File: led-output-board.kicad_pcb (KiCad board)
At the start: 2 copper layers, 29 parts, among them J1 DBT50G-9.5-2P, J10 DB301V-3.5-3P-GN, J2 Conn_02x08_Odd_Even, J3 DB301V-3.5-3P-GN, J4 DB301V-3.5-3P-GN, J5 DB301V-3.5-3P-GN, J6 DB301V-3.5-3P-GN, J7 DB301V-3.5-3P-GN, J8 DB301V-3.5-3P-GN, J9 DB301V-3.5-3P-GN, U1 SN74LVC8T245PWR

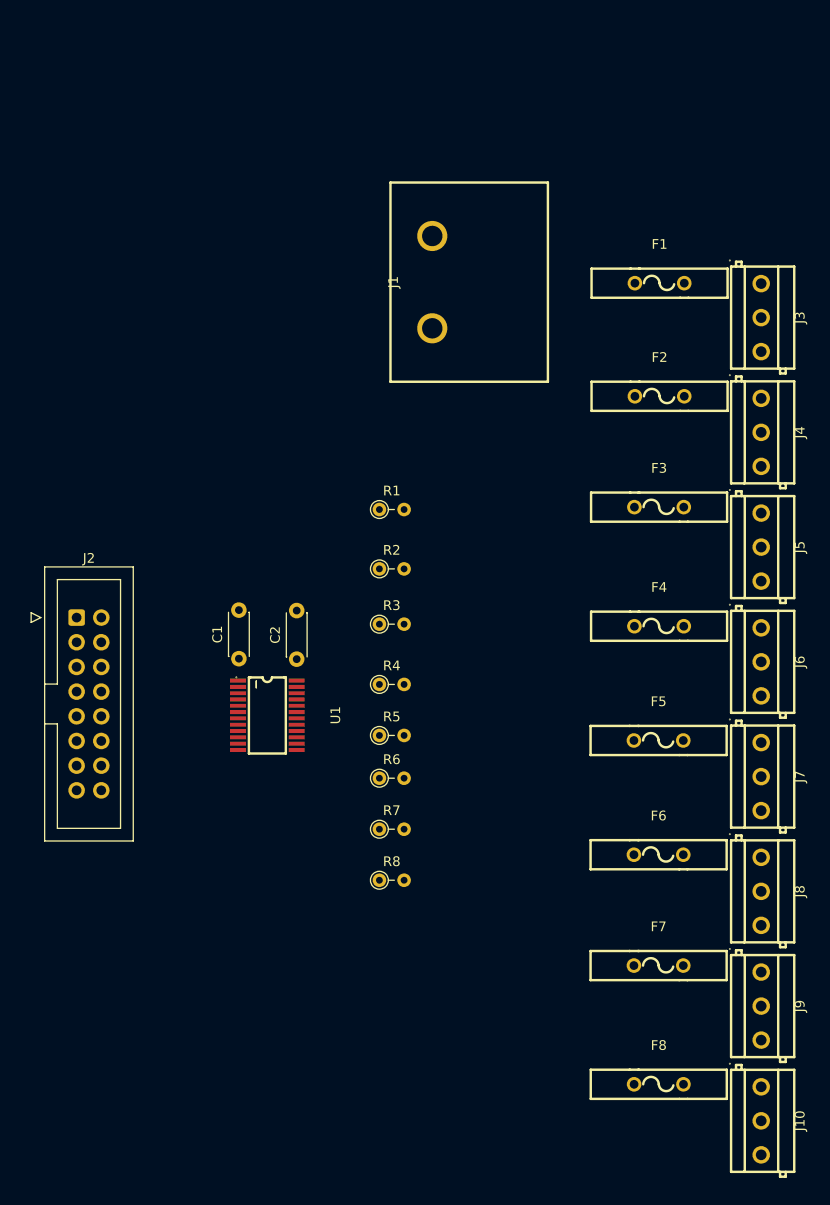
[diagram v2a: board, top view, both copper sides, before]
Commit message: Added pour for VIN
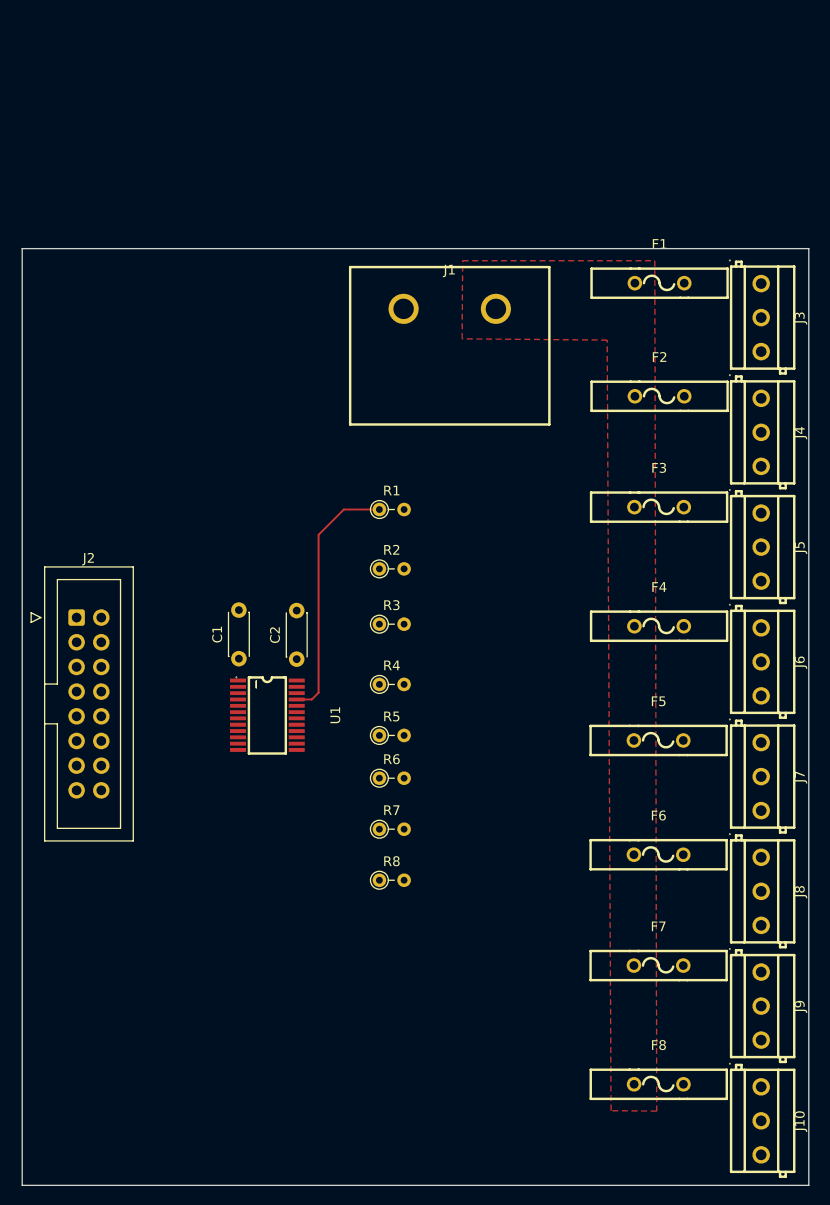
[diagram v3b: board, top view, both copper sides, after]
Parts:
- moved J1 3.29 mm to (105.7, 71.4), turned to 0 degrees
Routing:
- net Net-(U1-B1): track 0.00 -> 26.1 mm
- added copper zone on F.Cu, net +VIN
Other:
- board outline added: 80.9 x 96.4 mm
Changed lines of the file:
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@@
 	(footprint "easyeda2kicad:CONN-TH_2P-P9.50_DBT50G-9.5-2P"
 		(layer "F.Cu")
-		(at 103.85 68.65 90)
+		(at 105.65 71.4)
 		(property "Reference" "J1"
-			(at 0 -4 90)
+			(at 0 -4 0)
 			(layer "F.SilkS")
 			(effects
@@
 		)
 		(property "Value" "DBT50G-9.5-2P"
-			(at 0 4 90)
+			(at 0 4 0)
 			(layer "F.Fab")
 			(effects
@@
 		)
 		(property "Datasheet" ""
-			(at 0 0 90)
+			(at 0 0 0)
 			(layer "F.Fab")
 			(hide yes)
@@
 		)
 		(property "Description" ""
-			(at 0 0 90)
+			(at 0 0 0)
 			(layer "F.Fab")
 			(hide yes)
@@
 		)
 		(property "LCSC Part" ""
-			(at 0 0 90)
+			(at 0 0 0)
 			(layer "F.Fab")
 			(hide yes)
@@
 		(duplicate_pad_numbers_are_jumpers no)
 		(fp_line
-			(start 10.25 -4.3)
-			(end -10.25 -4.3)
+			(start -10.25 -4.3)
+			(end -10.25 11.9)
 			(stroke
 				(width 0.25)
@@
 		)
 		(fp_line
-			(start -10.25 -4.3)
-			(end -10.25 11.9)
+			(start -10.25 11.9)
+			(end 10.25 11.9)
 			(stroke
 				(width 0.25)
@@
 		)
 		(fp_line
-			(start 10.25 11.9)
-			(end 10.25 -4.3)
+			(start 10.25 -4.3)
+			(end -10.25 -4.3)
 			(stroke
 				(width 0.25)
@@
 		)
 		(fp_line
-			(start -10.25 11.9)
-			(end 10.25 11.9)
+			(start 10.25 11.9)
+			(end 10.25 -4.3)
 			(stroke
 				(width 0.25)
@@
 		)
 		(fp_line
-			(start 10.25 -4.3)
-			(end 10.25 11.9)
+			(start -10.25 -4.3)
+			(end 10.25 -4.3)
 			(stroke
 				(width 0.05)
@@
 		)
 		(fp_line
-			(start -10.25 -4.3)
-			(end 10.25 -4.3)
+			(start -10.25 11.9)
+			(end -10.25 -4.3)
 			(stroke
 				(width 0.05)
@@
 		)
 		(fp_line
-			(start 10.25 11.9)
-			(end -10.25 11.9)
+			(start 10.25 -4.3)
+			(end 10.25 11.9)
 			(stroke
 				(width 0.05)
@@
 		)
 		(fp_line
-			(start -10.25 11.9)
-			(end -10.25 -4.3)
+			(start 10.25 11.9)
+			(end -10.25 11.9)
 			(stroke
 				(width 0.05)
@@
 		)
 		(fp_text user "${REFERENCE}"
-			(at 0 0 90)
+			(at 0 0 0)
 			(layer "F.Fab")
 			(effects
@@
 		)
 		(pad "1" thru_hole circle
-			(at -4.75 0 90)
+			(at -4.75 0)
 			(size 3.1 3.1)
 			(drill 2.100022)
@@
 		)
 		(pad "2" thru_hole circle
-			(at 4.75 0 90)
+			(at 4.75 0)
 			(size 3.1 3.1)
 			(drill 2.100022)
@@
 			)
 		)
+	)
+	(gr_rect
+		(start 61.65 65.2)
+		(end 142.6 161.6)
+		(stroke
+			(width 0.05)
+			(type default)
+		)
+		(fill no)
+		(layer "Edge.Cuts")
+	)
+	(segment
+		(start 92.15 94.65)
+		(end 94.75 92.05)
+		(width 0.2)
+		(layer "F.Cu")
+		(net "Net-(U1-B1)")
+	)
+	(segment
+		(start 91.45 111.6)
+		(end 92.15 110.9)
+		(width 0.2)
+		(layer "F.Cu")
+		(net "Net-(U1-B1)")
+	)
+	(segment
+		(start 92.15 110.9)
+		(end 92.15 94.65)
+		(width 0.2)
+		(layer "F.Cu")
+		(net "Net-(U1-B1)")
+	)
+	(segment
+		(start 89.9 111.6)
+		(end 91.45 111.6)
+		(width 0.2)
+		(layer "F.Cu")
+		(net "Net-(U1-B1)")
+	)
+	(segment
+		(start 94.75 92.05)
+		(end 98.41 92.05)
+		(width 0.2)
+		(layer "F.Cu")
+		(net "Net-(U1-B1)")
+	)
+	(zone
+		(net "+VIN")
+		(layer "F.Cu")
+		(name "VIN")
+		(hatch edge 0.5)
+		(connect_pads
+			(clearance 0.5)
+		)
+		(min_thickness 0.25)
+		(fill
+			(thermal_gap 0.5)
+			(thermal_bridge_width 0.5)
+			(island_removal_mode 0)
+		)
+		(polygon
+			(pts
+				(xy 106.974844 66.45) (xy 126.75 66.45) (xy 126.950022 153.959616) (xy 122.250073 153.914424) (xy 121.850065 74.612767)
+				(xy 106.924933 74.485744)
+			)
+		)

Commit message: Widened and filled zone
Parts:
- moved F7 0.43 mm to (127.3, 139.4)
- moved F3 0.35 mm to (127.2, 92.2)
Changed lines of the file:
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@@
 	(footprint "easyeda2kicad:FUSE-TH_L14.0-W3.0-P5.08-D0.6"
 		(layer "F.Cu")
-		(at 127.1925 91.803929)
+		(at 127.21 92.15)
 		(property "Reference" "F3"
 			(at 0 -4 0)
@@
 	(footprint "easyeda2kicad:FUSE-TH_L14.0-W3.0-P5.08-D0.6"
 		(layer "F.Cu")
-		(at 127.1425 138.9825)
+		(at 127.26 139.4)
 		(property "Reference" "F7"
 			(at 0 -4 0)
@@
 		)
 		(min_thickness 0.25)
-		(fill
+		(fill yes
 			(thermal_gap 0.5)
 			(thermal_bridge_width 0.5)
@@
 		(polygon
 			(pts
-				(xy 106.974844 66.45) (xy 126.75 66.45) (xy 126.950022 153.959616) (xy 122.250073 153.914424) (xy 121.850065 74.612767)
-				(xy 106.924933 74.485744)
+				(xy 106.971117 67.05) (xy 126.751371 67.05) (xy 126.950022 153.959616) (xy 121.366483 153.905928)
+				(xy 116.35 110.85) (xy 115.9 76.8) (xy 106.909825 76.918169)
 			)
 		)
